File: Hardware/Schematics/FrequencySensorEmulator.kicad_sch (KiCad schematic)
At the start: 2 parts, among them U1 STM32G473CBTx, U2 LM4040DBZ-2.0

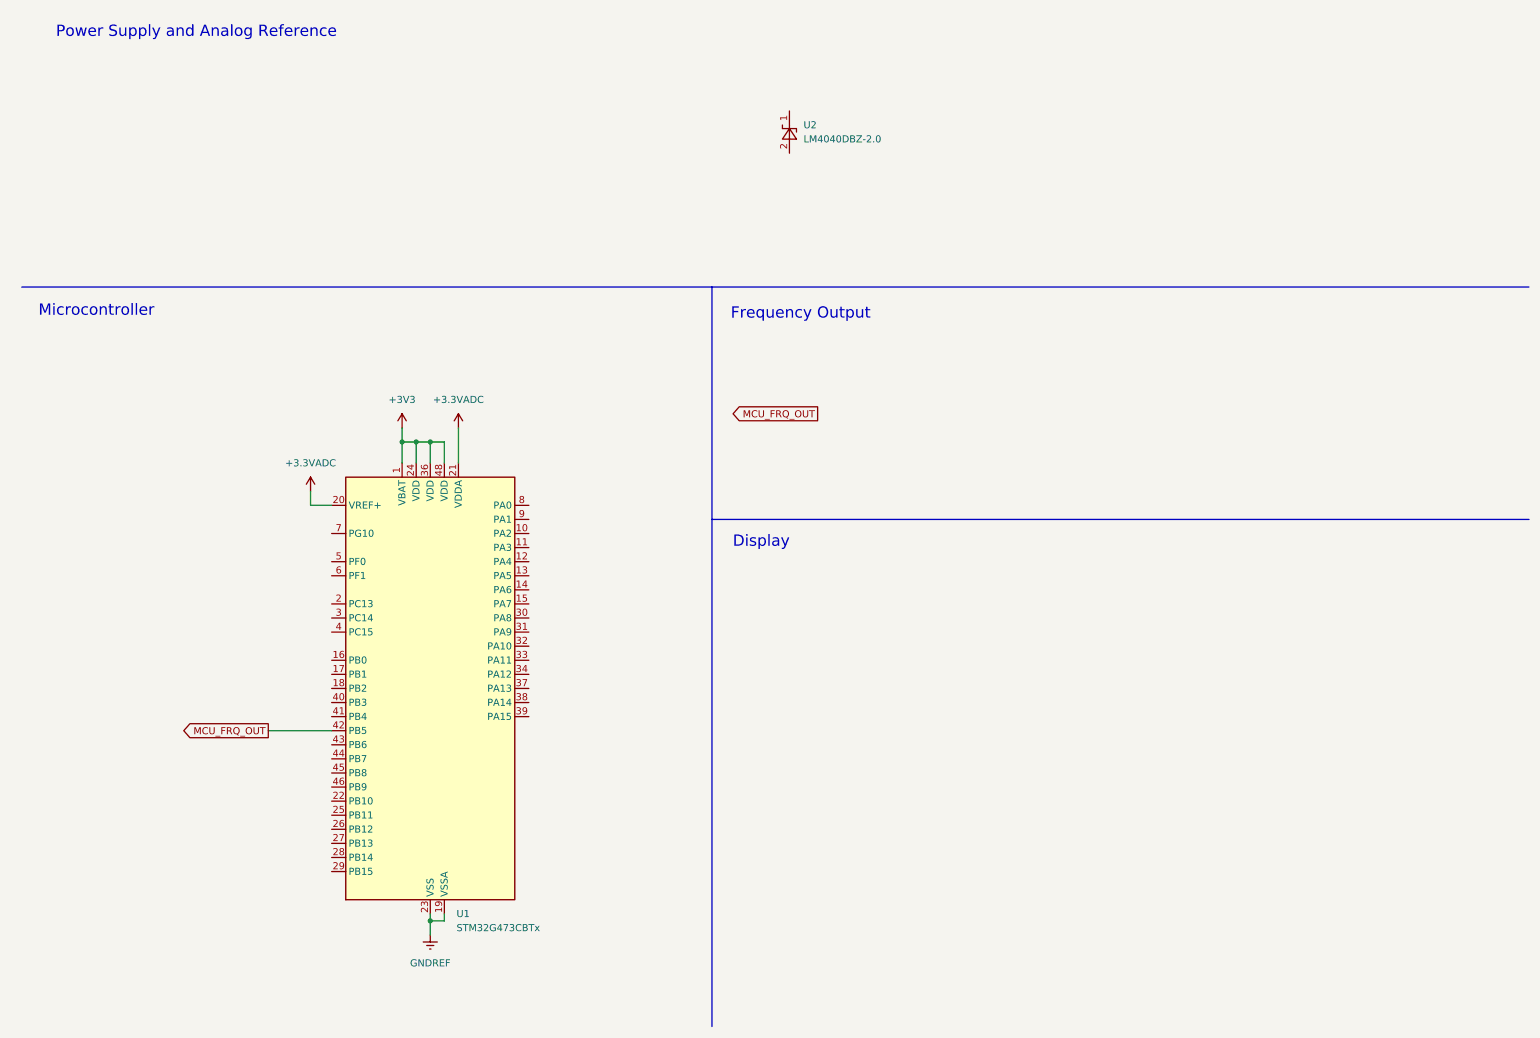
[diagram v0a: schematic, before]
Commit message: Sch: User inputs + MCU label connections
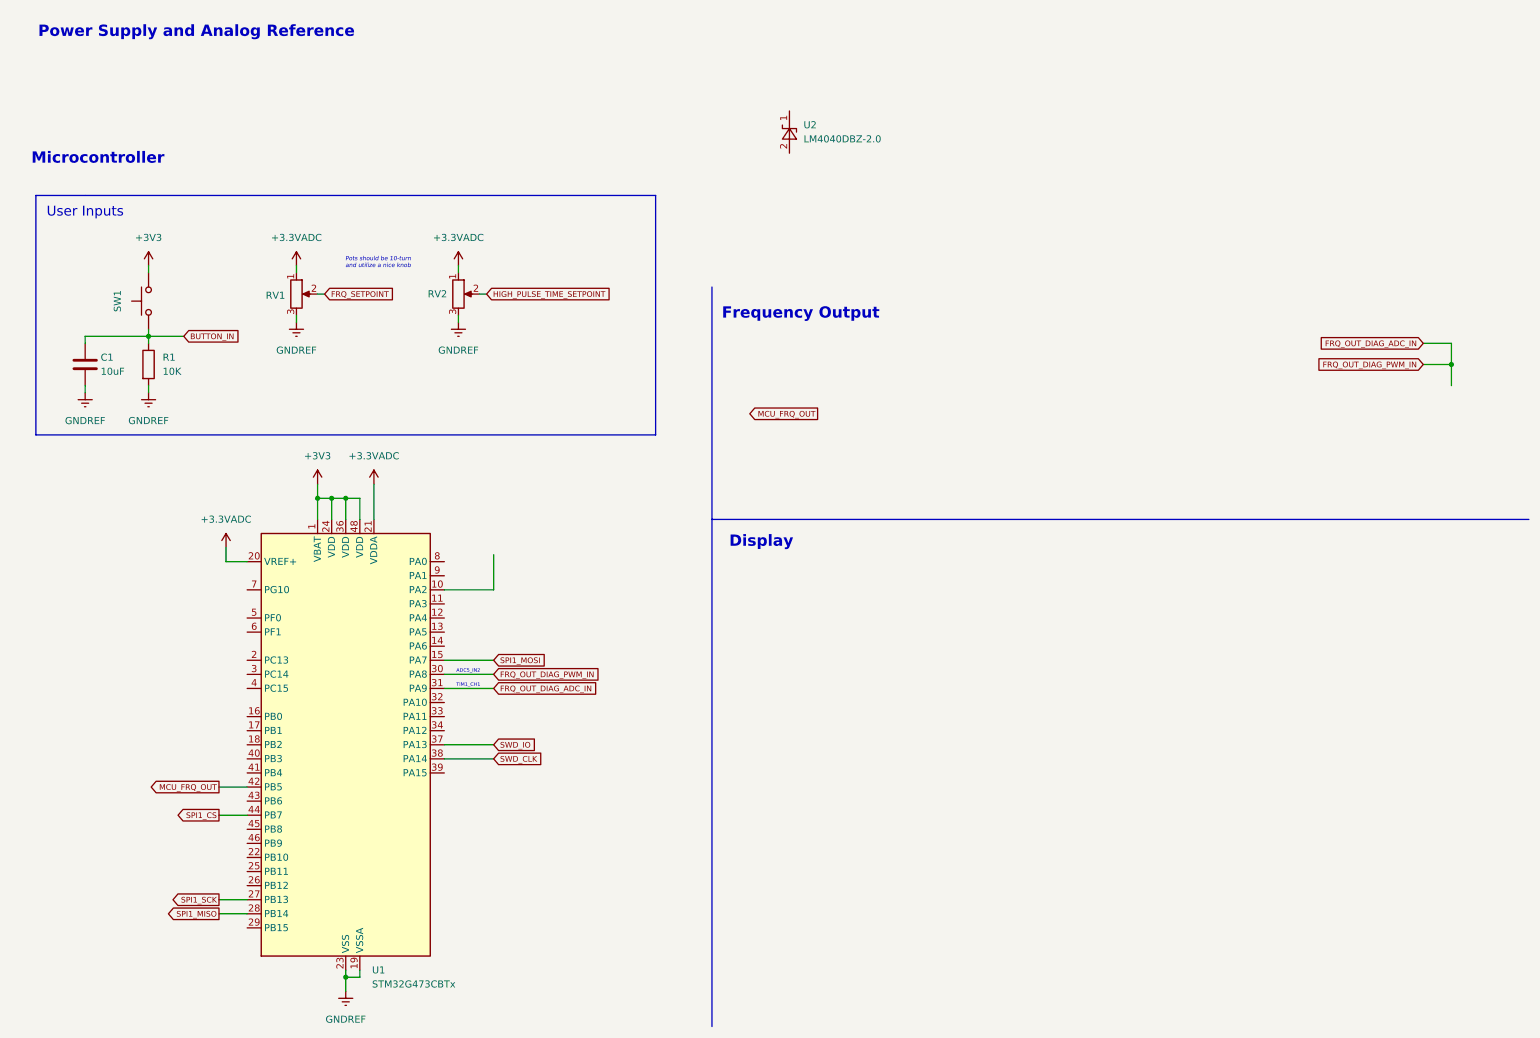
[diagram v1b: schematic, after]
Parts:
- added C1: 10uF, symbol Device:C
- added R1: 10K, symbol Device:R
- added RV1, RV2: R_Potentiometer, symbol Device:R_Potentiometer
- added SW1: SW_Push, symbol Switch:SW_Push
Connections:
- net +3.3VADC: now also RV1.1, RV2.1
- net +3V3: now also SW1.2
- net GNDREF: now also C1.2, R1.2, RV1.3, RV2.3
- net SPI1_MOSI: now reaches U1.15 (PA7)
- net SPI1_SCK: now reaches U1.27 (PB13)
- net SPI1_MISO: now reaches U1.28 (PB14)
- net FRQ_OUT_DIAG_ADC_IN: now reaches U1.30 (PA8)
- net FRQ_OUT_DIAG_ADC_IN: now also U1.31 (PA9)
- net SWD_IO: now reaches U1.37 (PA13)
- net SWD_CLK: now reaches U1.38 (PA14)
- net SPI1_CS: now reaches U1.44 (PB7)
- new net BUTTON_IN: C1.1, R1.1, SW1.1
- new net FRQ_SETPOINT: RV1.2
- new net HIGH_PULSE_TIME_SETPOINT: RV2.2
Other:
- note added: "ADC5_IN2"
- note added: "Pots should be 10-turn and utilize a nice knob"
- note added: "TIM1_CH1"
- note added: "User Inputs"
- company: (none) -> Abdulla Almosalami
- moved on the sheet: U1

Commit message: Added `Display` and `UserInputs` sch pg's; I/O
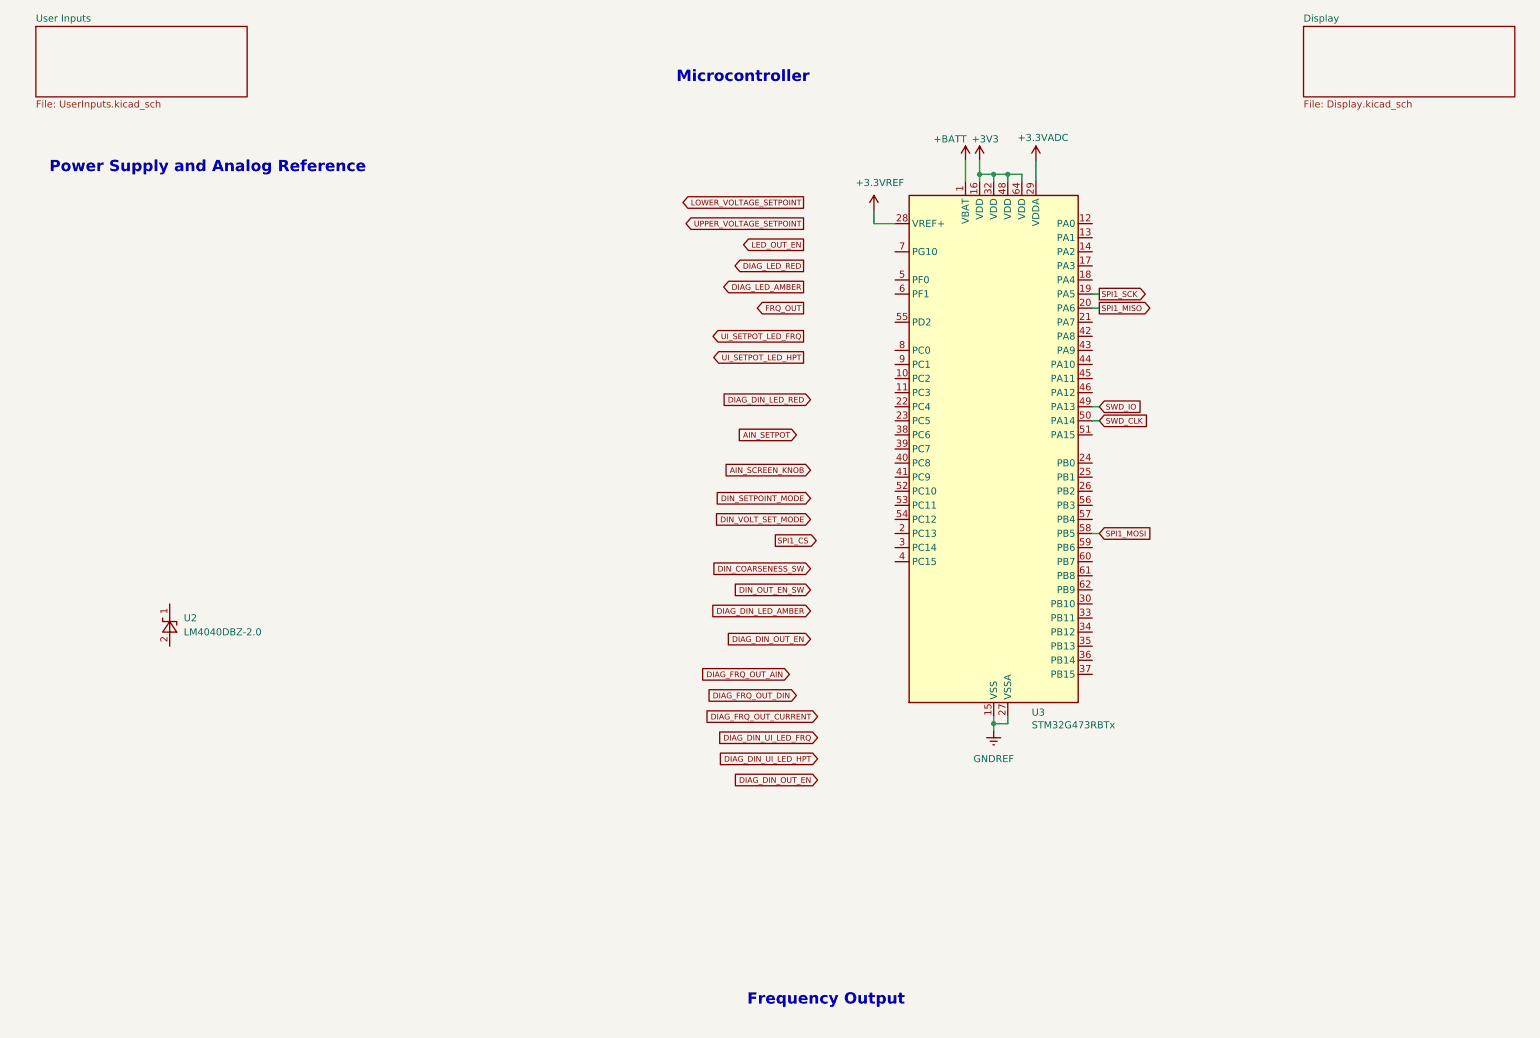
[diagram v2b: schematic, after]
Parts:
- removed C1: 10uF, symbol Device:C
- removed R1: 10K, symbol Device:R
- removed RV1, RV2: R_Potentiometer, symbol Device:R_Potentiometer
- removed SW1: SW_Push, symbol Switch:SW_Push
- removed U1: STM32G473CBTx, Package_QFP:LQFP-48_7x7mm_P0.5mm, symbol MCU_ST_STM32G4:STM32G473CBTx
- added U3: STM32G473RBTx, Package_QFP:LQFP-64_10x10mm_P0.5mm, symbol MCU_ST_STM32G4:STM32G473RBTx
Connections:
- net +3.3VADC: now also U3.29 (VDDA)
- net +3V3: now also U3.16 (VDD), U3.32 (VDD), U3.48 (VDD), U3.64 (VDD)
- net GNDREF: now also U3.15 (VSS), U3.27 (VSSA), U3.31 (VSS), U3.47 (VSS), U3.63 (VSS)
- net SPI1_MISO: now also U3.20 (PA6)
- net SPI1_MOSI: now also U3.58 (PB5)
- net SPI1_SCK: now also U3.19 (PA5)
- net SWD_CLK: now also U3.50 (PA14)
- net SWD_IO: now also U3.49 (PA13)
- new net +3.3VREF: U3.28 (VREF+)
- new net +BATT: U3.1 (VBAT)
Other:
- added sheet Display (Display.kicad_sch)
- added sheet User Inputs (UserInputs.kicad_sch)
- note removed: "ADC5_IN2"
- note removed: "Display"
- note removed: "Pots should be 10-turn and utilize a nice knob"
- note removed: "TIM1_CH1"
- note removed: "User Inputs"
- moved on the sheet: U2

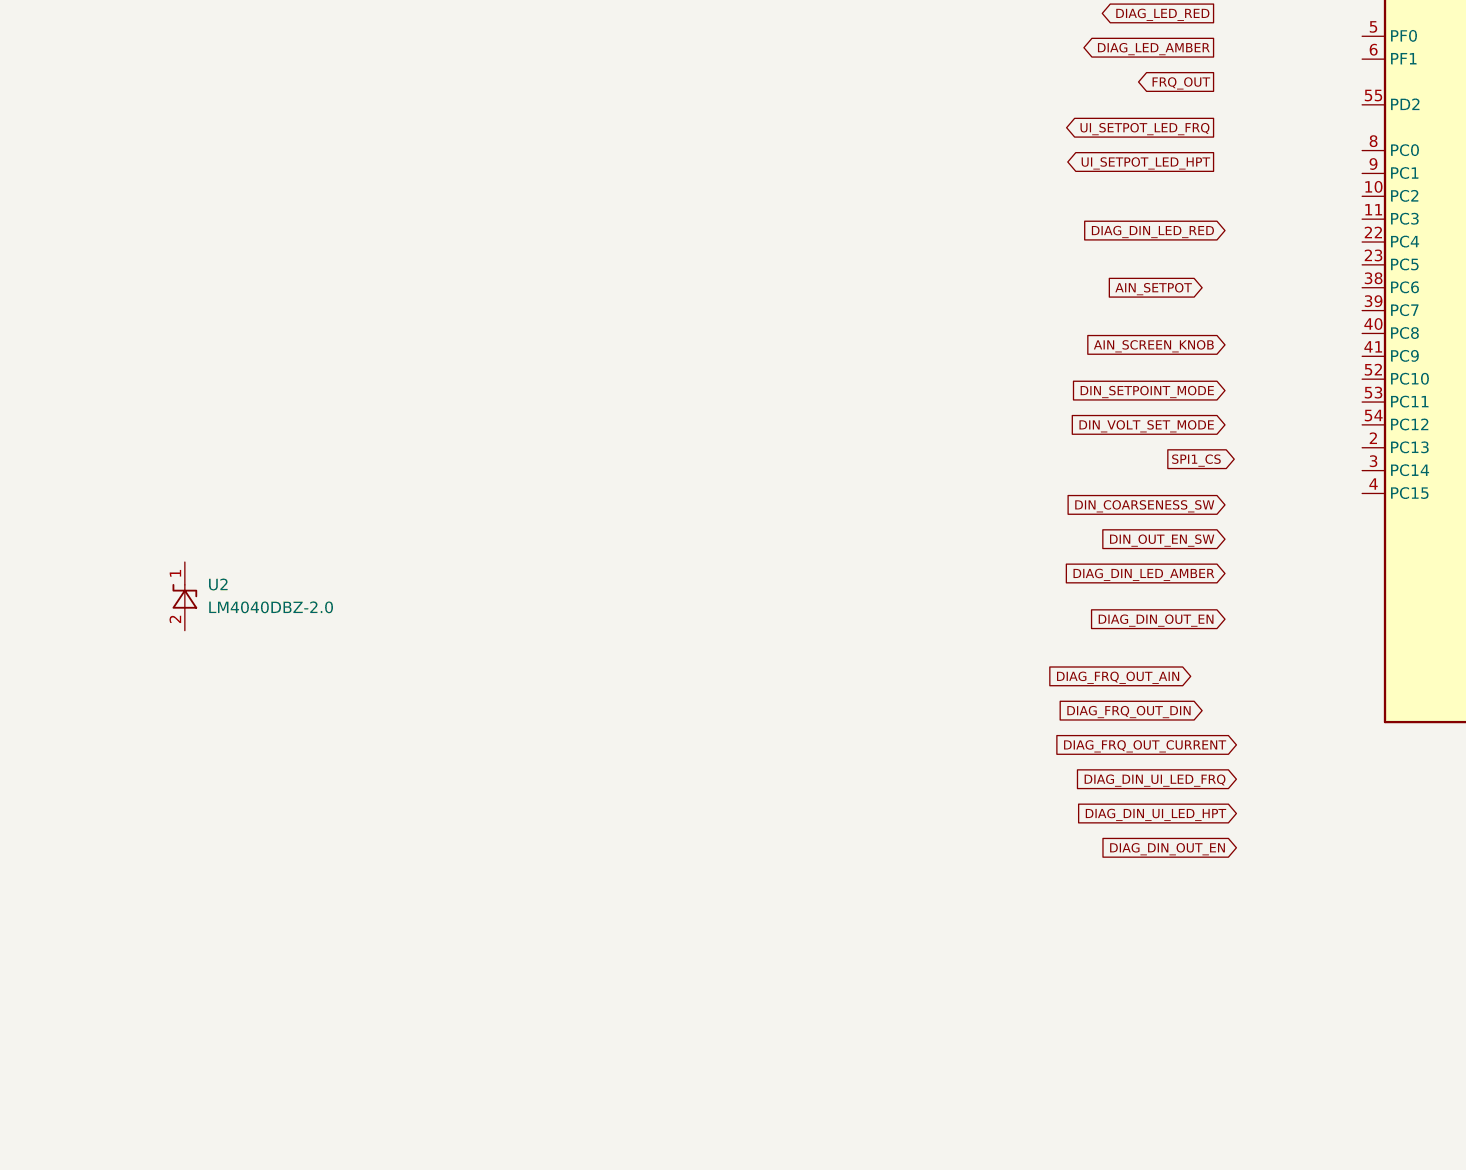
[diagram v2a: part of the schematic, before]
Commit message: Added `LT3085` to sch from shared lib repo
Added to `README.md` some of the relevant details.
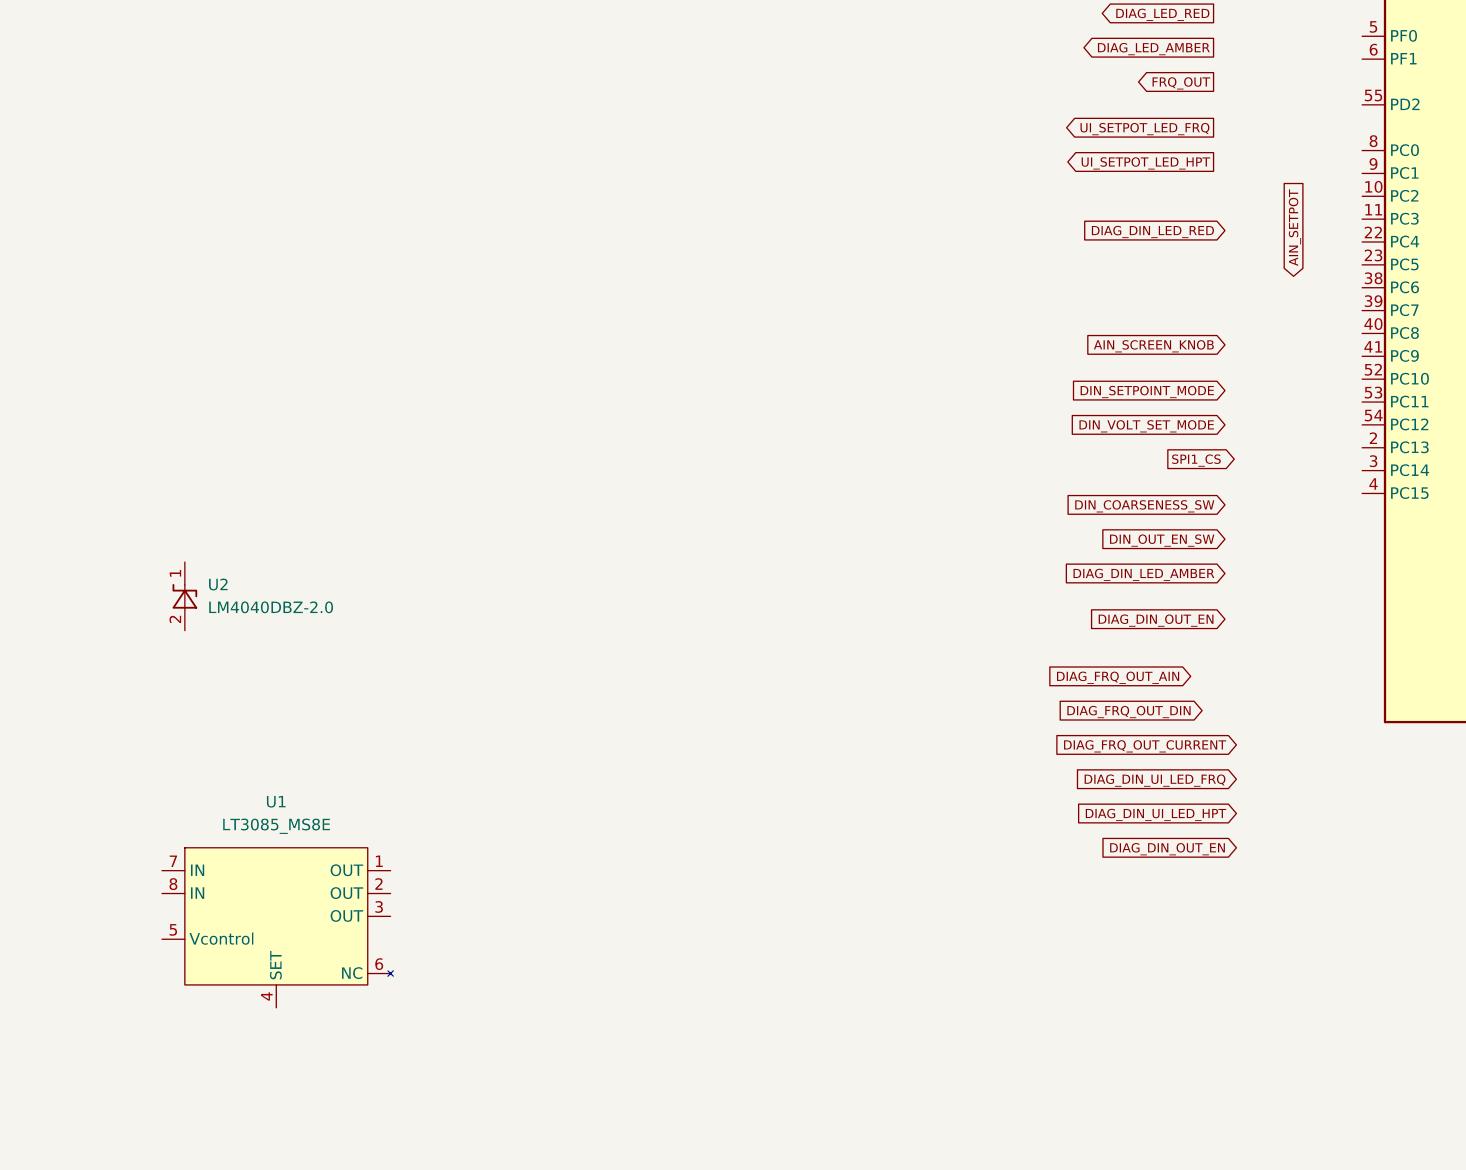
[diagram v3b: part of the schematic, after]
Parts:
- added U1: LT3085_MS8E, symbol Custom_VoltageRegulators:LT3085_MS8E
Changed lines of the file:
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@@
 	(global_label "AIN_SETPOT"
 		(shape input)
-		(at 152.4 90.17 180)
-		(fields_autoplaced yes)
-		(effects
-			(font
-				(size 1.016 1.016)
-			)
-			(justify right)
-		)
-		(property "Intersheetrefs" "${INTERSHEET_REFS}"
-			(at 141.3035 90.17 0)
-			(effects
-				(font
-					(size 1.27 1.27)
-				)
-				(justify right)
+		(at 162.56 88.9 90)
+		(fields_autoplaced yes)
+		(effects
+			(font
+				(size 1.016 1.016)
+			)
+			(justify left)
+		)
+		(property "Intersheetrefs" "${INTERSHEET_REFS}"
+			(at 162.56 77.8035 90)
+			(effects
+				(font
+					(size 1.27 1.27)
+				)
+				(justify left)
 				(hide yes)
 			)
@@
 					(unit 1)
 				)
+			)
+		)
+	)
+	(symbol
+		(lib_id "Custom_VoltageRegulators:LT3085_MS8E")
+		(at 49.53 160.02 0)
+		(unit 1)
+		(exclude_from_sim no)
+		(in_bom yes)
+		(on_board yes)
+		(dnp no)
+		(fields_autoplaced yes)
+		(property "Reference" "U1"
+			(at 49.53 147.32 0)
+			(effects
+				(font
+					(size 1.27 1.27)
+				)
+			)
+		)
+		(property "Value" "LT3085_MS8E"
+			(at 49.53 149.86 0)
+			(effects
+				(font
+					(size 1.27 1.27)
+				)
+			)
+		)
+		(property "Footprint" ""
+			(at 49.53 160.02 0)
+			(effects
+				(font
+					(size 1.27 1.27)
+				)
+				(hide yes)
+			)
+		)
+		(property "Datasheet" "https://www.analog.com/media/en/technical-documentation/data-sheets/lt3085.pdf"
+			(at 49.276 176.784 0)
+			(effects
+				(font
+					(size 1.27 1.27)
+				)
+				(hide yes)
+			)
+		)
+		(property "Description" "Adjustable 500mA Single Resistor Low Dropout Regulator (0 - 36V Output)"
+			(at 49.784 145.288 0)
+			(effects
+				(font
+					(size 1.27 1.27)
+				)
+				(hide yes)
+			)
+		)
+		(pin "7"
+		)
+		(pin "6"
+		)
+		(pin "4"
+		)
+		(pin "2"
+		)
+		(pin "1"
+		)
+		(pin "3"
+		)
+		(pin "8"
+		)
+		(pin "5"
+		)
+		(instances
+			(project ""
+				(path "/76d3015e-4ea5-4582-8e1b-ccd12abc8f3a"
+					(reference "U1")
+					(unit 1)
+				)
